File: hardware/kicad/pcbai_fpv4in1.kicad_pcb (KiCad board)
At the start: 8 copper layers, 100 x 100 mm, 585 parts, among them J1 BATT_PAD, J10 VSUP_5V_TBD, J11 TPS3700_VMOTOR_27V_18V, J12 BM06B-SRSS-TB, J13 TLV76733DRVR, J14 SM08B-SRSS-TB, J15 USBLC6-2SC6, J16 USBLC6-2SC6, J17 USBLC6-2SC6, J18 AT32F421K8T7, J19 DRV8300DRGER, J2 TPS54560DDAR, J20 INA186A3IDCKR, J21 INA186A3IDCKR, J22 INA186A3IDCKR, J23 AT32F421K8T7, J24 DRV8300DRGER, J25 INA186A3IDCKR, J26 INA186A3IDCKR, J27 INA186A3IDCKR, J28 AT32F421K8T7, J29 DRV8300DRGER, J3 TPS54560DDAR, J30 INA186A3IDCKR, J31 INA186A3IDCKR, J32 INA186A3IDCKR, J33 AT32F421K8T7, J34 DRV8300DRGER, J35 INA186A3IDCKR, J36 INA186A3IDCKR, J37 INA186A3IDCKR, J4 TPS54560DDAR, J5 AOZ1284PI, J6 AOZ1284PI, J7 TPS259251DRCR, J8 TPS259251DRCR, J9 TPS259251DRCR, Q1 BSC014N06NS, Q10 AOTL66912, Q11 AOTL66912, Q12 AOTL66912, Q13 AOTL66912, Q14 AOTL66912, Q15 AOTL66912, Q16 AOTL66912, Q17 AOTL66912, Q18 AOTL66912, Q19 AOTL66912, Q2 BSC014N06NS, Q20 AOTL66912, Q21 AOTL66912, Q22 AOTL66912, Q23 AOTL66912, Q24 AOTL66912, Q25 AOTL66912, Q26 AOTL66912, Q27 AOTL66912, Q28 AOTL66912, Q3 BSC014N06NS, Q4 BSC014N06NS, Q5 AOTL66912, Q6 AOTL66912, Q7 AOTL66912, Q8 AOTL66912, Q9 AOTL66912, U1 ACS770ECB-200B-PFF-T, U10 74LVC1G08, U11 TL431LI, U12 LM393, U13 74LVC1G08, U2 TL431LI, U3 LM393, U4 74LVC1G08, U5 TL431LI, U6 LM393, U7 74LVC1G08, U8 TL431LI, U9 LM393

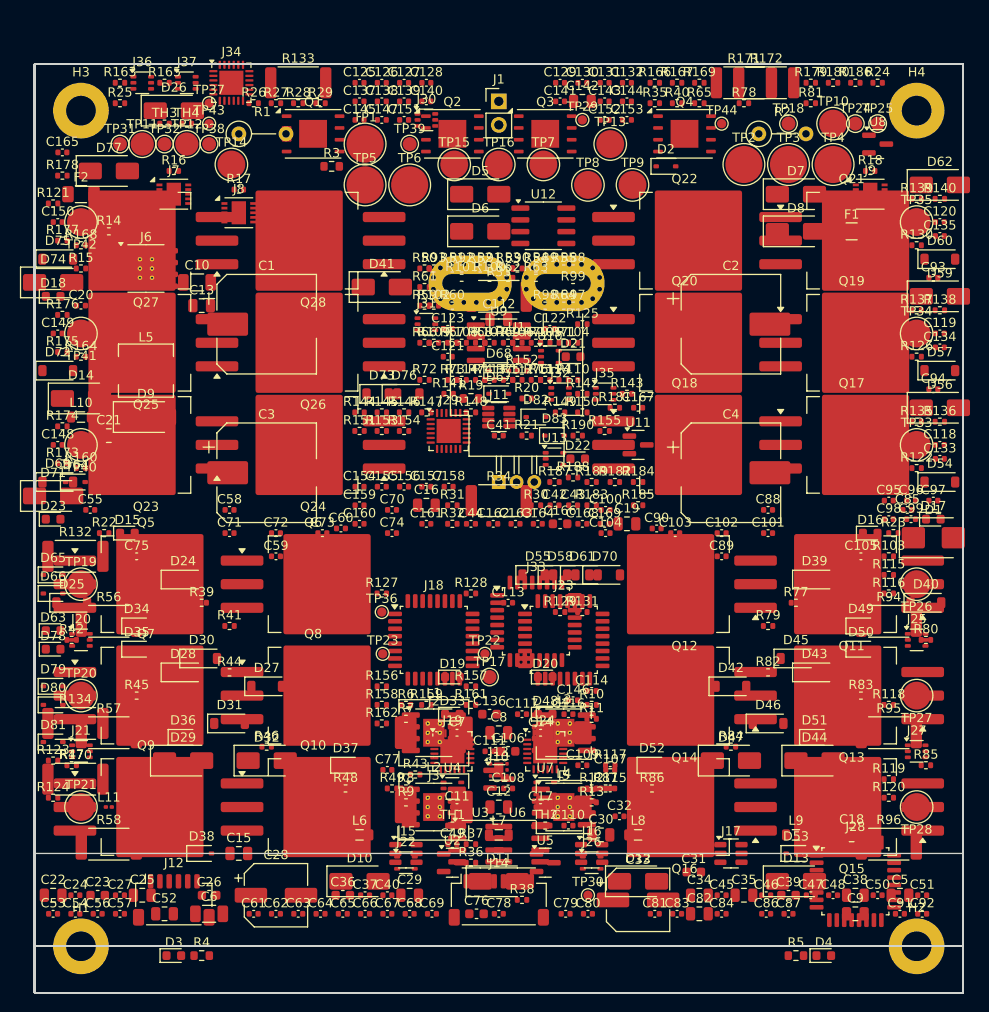
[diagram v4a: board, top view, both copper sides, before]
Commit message: PR-CH3: CH3 = 180°-rot(CH1) about (50, 50) + 3 sims (Task #76) (#54)
Tenth of 11 sequential A4-* PRs.

Placement (all 87/88 pairs Δ=0.000mm; 1 disclosed D26):
- Q17-Q22 FETs at 180°-rot of Q5-Q10 → Y=44/32/20
- TP33/34/35 motor pads at X=95
- J28-J32 + U8-U10 + LEDs + TH3 + R132-R134 shunts via rot(CH1)
- 63 channel passives via mirror_ch1_to_ch234.py ch3
- New script: mirror_ch1_to_ch234.py supports all 3 channel transforms

Audit:
- verify_spec_diff: 87/88 PASS
- MOUNT-HOLE-CONFLICT: 0
- Total PAD-OVERLAP 696 vs master 523 = +173 (structural mirror inheritance)
- target.h md5 unchanged

Sims (3, real + 4-point evidence per R18):
1. verify_spec_diff CH1↔CH3: 87/88 pairs Δ=0.000mm PASS
2. Elmer FEM CH1+CH2+CH3 thermal: T_J 62.74°C
   (CH1 alone 62.67, +CH2 62.71, +CH3 62.74 — 3-channel symmetry payoff)
3. S21 coupling (scikit-rf): CH1↔CH3 -83.6dB, CH2↔CH3 -76.6dB, both ≤-40dB PASS

Spec deviations: NONE.

Co-authored-by: Sai Kishore Naidu <naidu.saikishore9@gmail.com>
Co-authored-by: Claude Opus 4.7 (1M context) <noreply@anthropic.com>
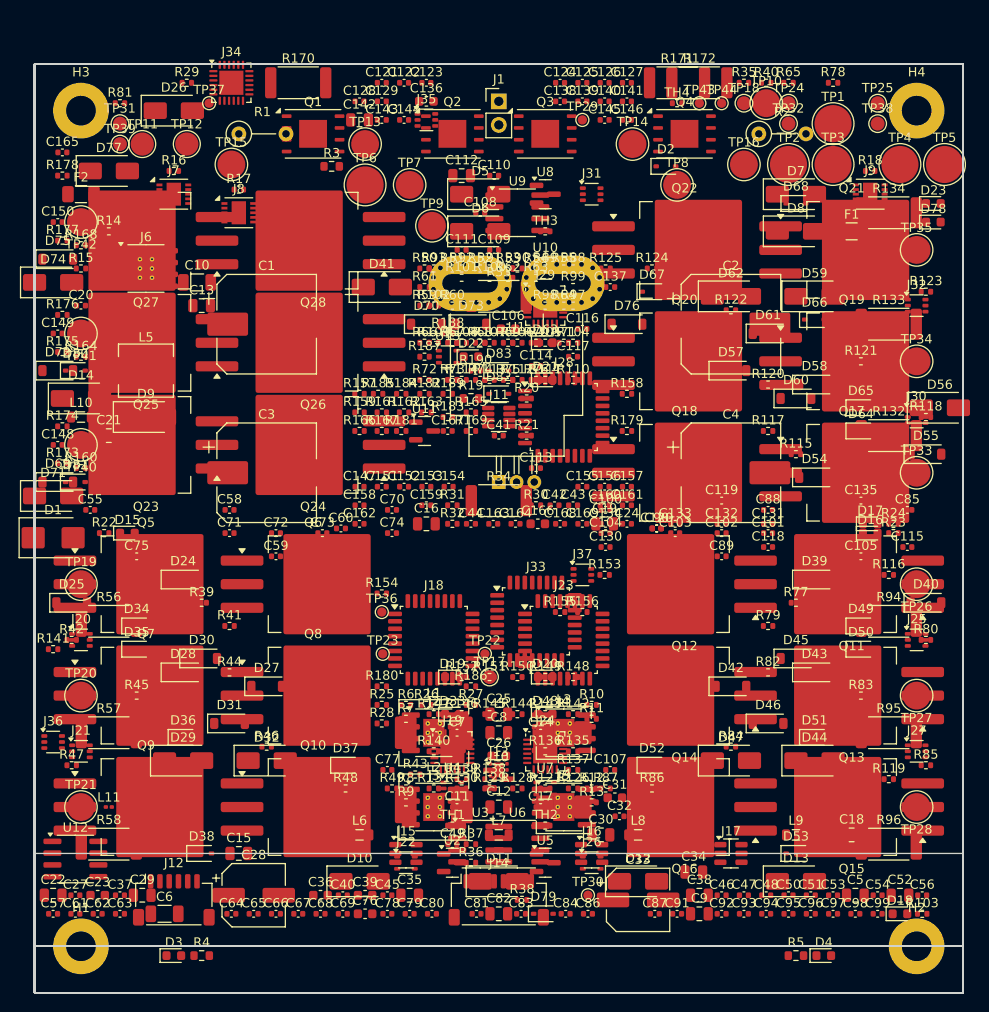
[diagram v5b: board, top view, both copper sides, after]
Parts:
- R126, R127, R128, R129, R130, R131, R135, R136, R137, R138, R139, R140, R142, R143, R144, R145, R146, R147, R148, R149, R150, R151, R152: moved to B.Cu
- moved D18 112.9 mm to (93.2, 91.5)
- moved R123 106.7 mm to (96.0, 24.5)
- moved D78 105.4 mm to (96.8, 17.0)
- moved R134 103.4 mm to (92.0, 16.0)
- moved D23 100.7 mm to (96.8, 15.0)
- moved D1 94.8 mm to (2.00, 51.0)
- moved D65 88.8 mm to (89.0, 37.0)
- moved C56 88.8 mm to (95.6, 89.5)
- moved R121 88.6 mm to (89.0, 32.0)
- moved R132 88.6 mm to (92.0, 40.0)
- moved D66 87.1 mm to (84.0, 27.5)
- moved C54 86.4 mm to (90.8, 89.5)
- moved R124 86.1 mm to (66.5, 22.0)
- moved U12 84.8 mm to (4.40, 85.6)
- moved D64 84.8 mm to (89.0, 39.5)
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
